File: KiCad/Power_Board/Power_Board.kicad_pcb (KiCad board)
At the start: 4 copper layers, 101.6 x 63.5 mm, 170 parts, among them P1 CONN_LEFT_TOP, P10 CONN_02X01, P2 CONN_RIGHT_TOP, P3 CONN_LEFT_BOTTOM, P4 CONN_RIGHT_BOTTOM, P5 CONN_02X01, P6 CONN_02X01, P7 CONN_02X01, P8 CONN_02X01, P9 CONN_02X01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

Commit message: SPI Trace Cleanup
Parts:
- added ?: , OpenCamera:STITCH_VIA, F.Cu at (102.3, 101.1)
- added ?: , OpenCamera:STITCH_VIA, F.Cu at (101.0, 101.3)
- added ?: , OpenCamera:STITCH_VIA, F.Cu at (99.4, 101.1)
- moved ? 14.0 mm to (144.5, 113.5)
- moved ? 7.57 mm to (146.3, 113.7)
- moved TP4 3.54 mm to (127.2, 123.1)
- moved TP1 2.85 mm to (127.3, 133.4)
- moved ? 2.02 mm to (171.7, 113.7)
- moved TP7 1.31 mm to (161.5, 115.2)
- moved R32 0.52 mm to (159.4, 111.9)
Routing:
- net /Digital_Power/5V: track 45.4 -> 9.83 mm
- net /Analog_Power/-15Va: track 40.3 -> 17.9 mm, vias 2 -> 1
- net /Analog_Power/50Va: track 45.8 -> 31.1 mm, vias 2 -> 1
- net /connectors/L8: track 97.9 -> 91.6 mm
- net /connectors/L6: track 103.7 -> 100.1 mm, vias 2 -> 3
- net /connectors/L5: track 98.4 -> 96.4 mm, vias 3 -> 2
- net /connectors/L9: track 105.4 -> 104.2 mm
- net Net-(C15-Pad1): track 14.8 -> 15.7 mm
- net /connectors/R10: track 16.3 -> 15.7 mm
- net /connectors/R9: track 18.8 -> 18.3 mm
- net Net-(C39-Pad1): track 17.5 -> 18.0 mm

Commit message: More SPI Cleanup.
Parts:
- moved TP7 4.15 mm to (163.9, 111.8)
- moved TP18 1.68 mm to (148.6, 113.2)
- moved TP25 1.37 mm to (156.7, 113.9)
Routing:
- net /connectors/L9: track 104.2 -> 100.3 mm
- net /connectors/L6: track 100.1 -> 101.2 mm
- net /connectors/L5: track 96.4 -> 97.5 mm
- net /connectors/L8: track 91.6 -> 92.6 mm

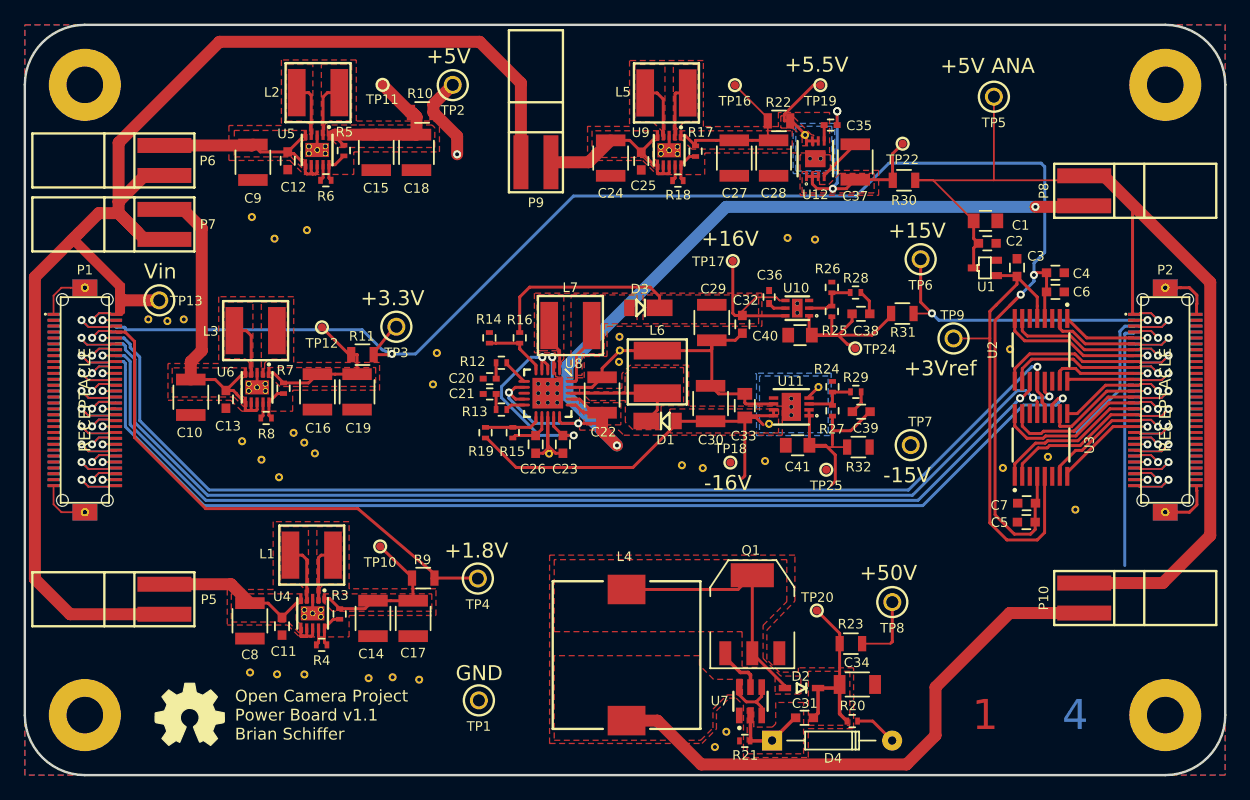
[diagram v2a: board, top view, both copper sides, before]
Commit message: Thickened Power Traces.
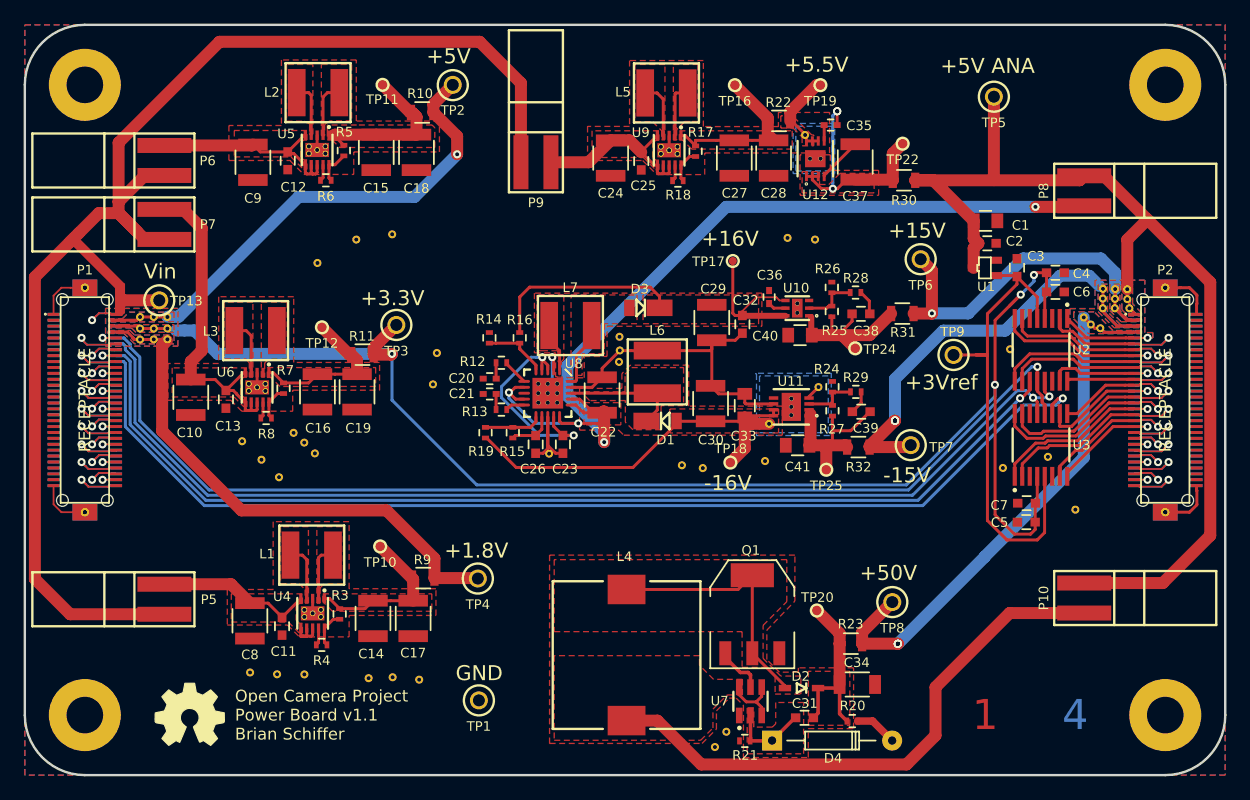
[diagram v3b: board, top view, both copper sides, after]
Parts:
- added ?: , OpenCamera:STITCH_VIA, F.Cu at (179.9, 101.9)
- added ?: , OpenCamera:STITCH_VIA, F.Cu at (182.4, 100.2)
- added ?: , OpenCamera:STITCH_VIA, F.Cu at (182.2, 99.4)
- added ?: , OpenCamera:STITCH_VIA, F.Cu at (101.0, 102.8)
- added ?: , OpenCamera:STITCH_VIA, F.Cu at (99.8, 102.8)
- added ?: , OpenCamera:STITCH_VIA, F.Cu at (98.7, 102.8)
- added ?: , OpenCamera:STITCH_VIA, F.Cu at (101.0, 101.9)
- added ?: , OpenCamera:STITCH_VIA, F.Cu at (99.8, 101.9)
- added ?: , OpenCamera:STITCH_VIA, F.Cu at (98.7, 101.9)
- added ?: , OpenCamera:STITCH_VIA, F.Cu at (179.1, 101.6)
- added ?: , OpenCamera:STITCH_VIA, F.Cu at (178.5, 101.0)
- added ?: , OpenCamera:STITCH_VIA, F.Cu at (180.1, 100.2)
- added ?: , OpenCamera:STITCH_VIA, F.Cu at (180.1, 99.4)
- added ?: , OpenCamera:STITCH_VIA, F.Cu at (180.1, 98.5)
- added ?: , OpenCamera:STITCH_VIA, F.Cu at (182.2, 98.6)
- added ?: , OpenCamera:STITCH_VIA, F.Cu at (181.2, 100.2)
- added ?: , OpenCamera:STITCH_VIA, F.Cu at (181.2, 99.4)
- added ?: , OpenCamera:STITCH_VIA, F.Cu at (181.2, 98.6)
- moved ? 7.22 mm to (120.0, 93.9)
- moved ? 6.92 mm to (117.0, 94.4)
- moved ? 6.78 mm to (113.7, 96.4)
- moved ? 3.70 mm to (98.7, 100.9)
- moved TP9 1.40 mm to (167.5, 104.1)
- moved ? 0.50 mm to (99.8, 100.9)
- moved ? 0.34 mm to (101.0, 100.9)
- moved TP3 0.15 mm to (120.3, 101.6)
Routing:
- net /Digital_Power/5V: track 9.83 -> 42.3 mm, vias 2 -> 1
- net /Analog_Power/-15Va: track 17.9 -> 40.8 mm, vias 1 -> 7
- net /Analog_Power/50Va: track 31.1 -> 50.0 mm, vias 1 -> 4
- net /Digital_Power/3.3V: track 144.1 -> 133.6 mm
- net /Analog_Power/5Va: track 98.4 -> 108.1 mm, vias 1 -> 0
- net Net-(C38-Pad1): track 17.4 -> 26.8 mm
- net Net-(C31-Pad1): track 15.1 -> 22.1 mm
- net Net-(C35-Pad1): track 20.3 -> 26.8 mm
- net Net-(C14-Pad1): track 13.9 -> 19.7 mm
- net /Analog_Power/15Va: track 26.2 -> 31.6 mm, vias 2 -> 1
- net /Analog_Power/5.5V: track 8.47 -> 12.0 mm
- net /Digital_Power/1.8V: track 49.1 -> 46.7 mm, vias 1 -> 0
- net Net-(C16-Pad1): track 13.7 -> 15.7 mm
- net Net-(C39-Pad1): track 18.0 -> 19.7 mm
- net /Analog_Power/-16V: track 36.2 -> 37.6 mm
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- added copper zone on B.Cu, net /Analog_Power/-15Va
- added copper zone on F.Cu, net /Analog_Power/-15Va
- added copper zone on B.Cu, net /Analog_Power/15Va
- added copper zone on F.Cu, net /Analog_Power/15Va
- added copper zone on B.Cu, net /Analog_Power/50Va
- added copper zone on F.Cu, net /Analog_Power/50Va
- added copper zone on B.Cu, net /Analog_Power/5Va
- added copper zone on F.Cu, net /Analog_Power/5Va
- added copper zone on B.Cu, net /Digital_Power/1.8V
- added copper zone on F.Cu, net /Digital_Power/1.8V
- added copper zone on B.Cu, net /Digital_Power/3.3V
- added copper zone on F.Cu, net /Digital_Power/3.3V
- added copper zone on B.Cu, net /Digital_Power/5V
- added copper zone on F.Cu, net /Digital_Power/5V

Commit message: Pulled ground pour back to ensure 20mil clearance to board edge.
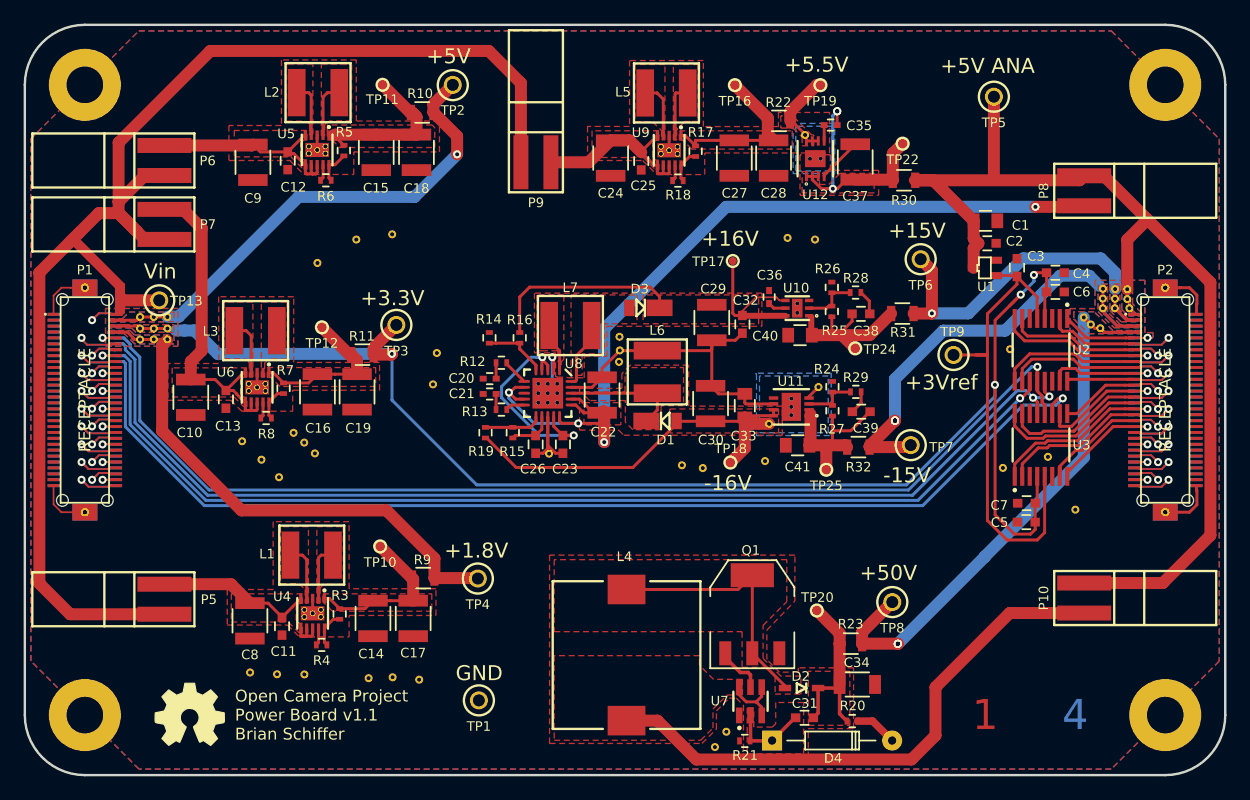
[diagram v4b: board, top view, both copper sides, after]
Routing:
- net Net-(C22-Pad1): track 81.0 -> 78.4 mm
- net /connectors/L1: track 151.5 -> 150.5 mm

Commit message: Placed a bunch of ground plane stitching vias.
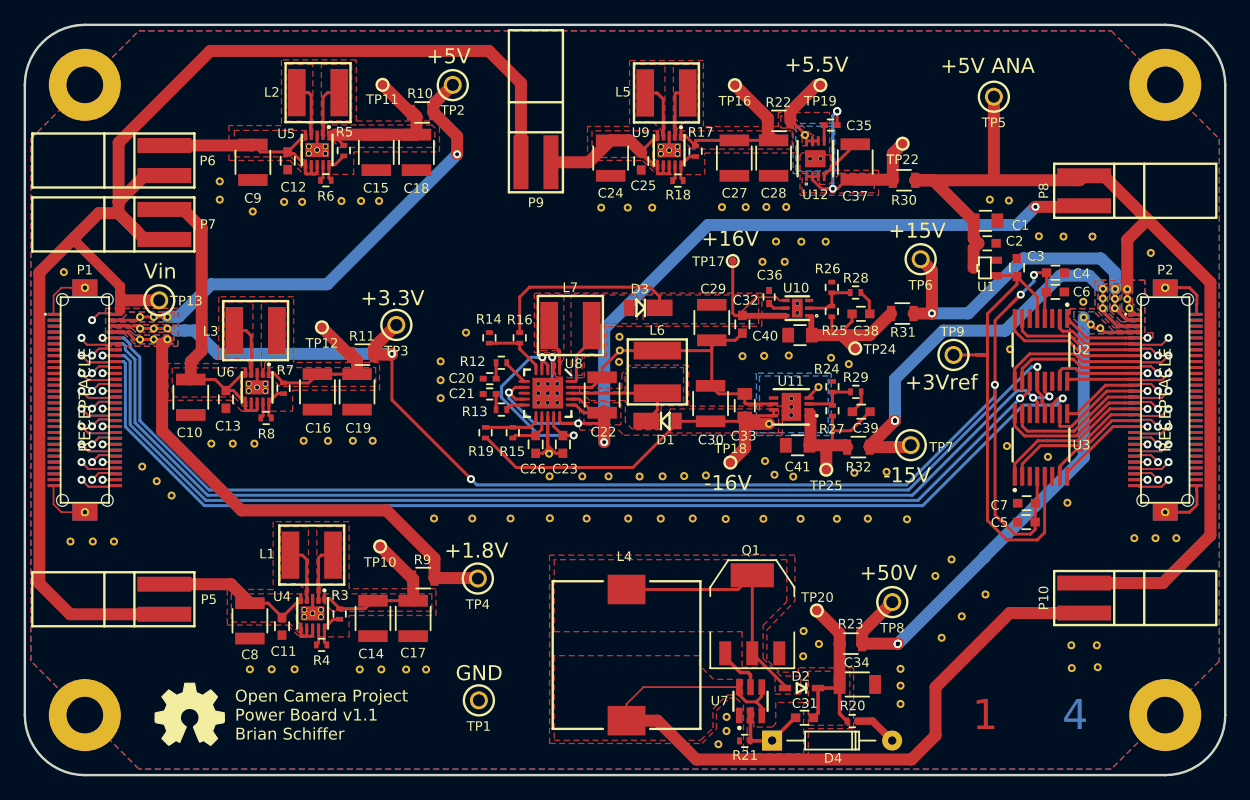
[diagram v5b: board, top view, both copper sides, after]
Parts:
- added ?: , OpenCamera:STITCH_VIA, F.Cu at (172.2, 91.1)
- added ?: , OpenCamera:STITCH_VIA, F.Cu at (172.0, 111.8)
- added ?: , OpenCamera:STITCH_VIA, F.Cu at (94.7, 119.9)
- added ?: , OpenCamera:STITCH_VIA, F.Cu at (96.4, 119.9)
- added ?: , OpenCamera:STITCH_VIA, F.Cu at (92.8, 119.9)
- added ?: , OpenCamera:STITCH_VIA, F.Cu at (182.8, 119.6)
- added ?: , OpenCamera:STITCH_VIA, F.Cu at (184.6, 119.6)
- added ?: , OpenCamera:STITCH_VIA, F.Cu at (186.4, 119.6)
- added ?: , OpenCamera:STITCH_VIA, F.Cu at (179.7, 130.6)
- added ?: , OpenCamera:STITCH_VIA, F.Cu at (177.5, 130.6)
- added ?: , OpenCamera:STITCH_VIA, F.Cu at (179.6, 128.7)
- added ?: , OpenCamera:STITCH_VIA, F.Cu at (170.6, 91.0)
- added ?: , OpenCamera:STITCH_VIA, F.Cu at (177.5, 128.7)
- added ?: , OpenCamera:STITCH_VIA, F.Cu at (163.0, 130.7)
- added ?: , OpenCamera:STITCH_VIA, F.Cu at (163.0, 132.1)
- added ?: , OpenCamera:STITCH_VIA, F.Cu at (163.0, 133.7)
- added ?: , OpenCamera:STITCH_VIA, F.Cu at (156.1, 128.6)
- added ?: , OpenCamera:STITCH_VIA, F.Cu at (154.8, 129.6)
- added ?: , OpenCamera:STITCH_VIA, F.Cu at (154.8, 127.5)
- added ?: , OpenCamera:STITCH_VIA, F.Cu at (148.3, 136.0)
- added ?: , OpenCamera:STITCH_VIA, F.Cu at (121.2, 130.8)
- added ?: , OpenCamera:STITCH_VIA, F.Cu at (153.9, 114.4)
- added ?: , OpenCamera:STITCH_VIA, F.Cu at (92.2, 97.1)
- added ?: , OpenCamera:STITCH_VIA, F.Cu at (157.1, 104.4)
- added ?: , OpenCamera:STITCH_VIA, F.Cu at (158.6, 104.9)
- added ?: , OpenCamera:STITCH_VIA, F.Cu at (153.2, 96.3)
- added ?: , OpenCamera:STITCH_VIA, F.Cu at (153.6, 104.2)
- added ?: , OpenCamera:STITCH_VIA, F.Cu at (151.5, 104.2)
- added ?: , OpenCamera:STITCH_VIA, F.Cu at (149.6, 104.2)
- added ?: , OpenCamera:STITCH_VIA, F.Cu at (156.7, 94.6)
- added ?: , OpenCamera:STITCH_VIA, F.Cu at (151.3, 96.3)
- added ?: , OpenCamera:STITCH_VIA, F.Cu at (153.3, 91.6)
- added ?: , OpenCamera:STITCH_VIA, F.Cu at (151.7, 91.6)
- added ?: , OpenCamera:STITCH_VIA, F.Cu at (184.2, 95.5)
- added ?: , OpenCamera:STITCH_VIA, F.Cu at (149.9, 91.6)
- added ?: , OpenCamera:STITCH_VIA, F.Cu at (147.9, 91.6)
- added ?: , OpenCamera:STITCH_VIA, F.Cu at (110.8, 91.2)
- added ?: , OpenCamera:STITCH_VIA, F.Cu at (142.0, 91.7)
- added ?: , OpenCamera:STITCH_VIA, F.Cu at (139.9, 91.7)
- added ?: , OpenCamera:STITCH_VIA, F.Cu at (137.7, 91.7)
- added ?: , OpenCamera:STITCH_VIA, F.Cu at (118.9, 91.1)
- added ?: , OpenCamera:STITCH_VIA, F.Cu at (108.2, 92.0)
- added ?: , OpenCamera:STITCH_VIA, F.Cu at (105.4, 91.0)
- added ?: , OpenCamera:STITCH_VIA, F.Cu at (105.4, 89.4)
- added ?: , OpenCamera:STITCH_VIA, F.Cu at (178.5, 99.6)
- added ?: , OpenCamera:STITCH_VIA, F.Cu at (101.3, 116.0)
- added ?: , OpenCamera:STITCH_VIA, F.Cu at (100.1, 114.8)
- added ?: , OpenCamera:STITCH_VIA, F.Cu at (98.8, 113.6)
- added ?: , OpenCamera:STITCH_VIA, F.Cu at (170.2, 124.4)
- added ?: , OpenCamera:STITCH_VIA, F.Cu at (167.3, 121.5)
- added ?: , OpenCamera:STITCH_VIA, F.Cu at (166.0, 122.8)
- added ?: , OpenCamera:STITCH_VIA, F.Cu at (163.6, 118.0)
- added ?: , OpenCamera:STITCH_VIA, F.Cu at (161.8, 114.0)
- added ?: , OpenCamera:STITCH_VIA, F.Cu at (159.1, 114.1)
- added ?: , OpenCamera:STITCH_VIA, F.Cu at (152.3, 114.3)
- added ?: , OpenCamera:STITCH_VIA, F.Cu at (179.3, 94.1)
- added ?: , OpenCamera:STITCH_VIA, F.Cu at (145.4, 118.0)
- added ?: , OpenCamera:STITCH_VIA, F.Cu at (160.2, 118.0)
- added ?: , OpenCamera:STITCH_VIA, F.Cu at (157.6, 118.0)
- added ?: , OpenCamera:STITCH_VIA, F.Cu at (142.7, 118.0)
- added ?: , OpenCamera:STITCH_VIA, F.Cu at (142.9, 114.4)
- added ?: , OpenCamera:STITCH_VIA, F.Cu at (140.9, 114.4)
- added ?: , OpenCamera:STITCH_VIA, F.Cu at (138.3, 114.4)
- added ?: , OpenCamera:STITCH_VIA, F.Cu at (136.1, 114.4)
- added ?: , OpenCamera:STITCH_VIA, F.Cu at (133.3, 114.4)
- added ?: , OpenCamera:STITCH_VIA, F.Cu at (126.2, 102.2)
- added ?: , OpenCamera:STITCH_VIA, F.Cu at (176.8, 94.1)
- added ?: , OpenCamera:STITCH_VIA, F.Cu at (124.1, 107.8)
- added ?: , OpenCamera:STITCH_VIA, F.Cu at (114.6, 111.4)
- added ?: , OpenCamera:STITCH_VIA, F.Cu at (148.2, 118.0)
- added ?: , OpenCamera:STITCH_VIA, F.Cu at (123.5, 118.0)
- added ?: , OpenCamera:STITCH_VIA, F.Cu at (133.3, 118.0)
- added ?: , OpenCamera:STITCH_VIA, F.Cu at (154.6, 118.0)
- added ?: , OpenCamera:STITCH_VIA, F.Cu at (151.4, 118.0)
- added ?: , OpenCamera:STITCH_VIA, F.Cu at (140.0, 118.0)
- added ?: , OpenCamera:STITCH_VIA, F.Cu at (136.4, 118.0)
- added ?: , OpenCamera:STITCH_VIA, F.Cu at (130.0, 118.0)
- added ?: , OpenCamera:STITCH_VIA, F.Cu at (174.7, 94.1)
- added ?: , OpenCamera:STITCH_VIA, F.Cu at (126.8, 118.0)
- added ?: , OpenCamera:STITCH_VIA, F.Cu at (166.5, 128.1)
- moved ? 13.0 mm to (168.2, 126.3)
- moved ? 8.10 mm to (112.4, 91.2)
- moved ? 6.42 mm to (117.4, 91.1)
- moved ? 5.00 mm to (118.3, 111.4)
- moved ? 4.12 mm to (116.7, 111.4)
- moved ? 3.53 mm to (108.3, 111.6)
- moved ? 3.50 mm to (115.7, 91.1)
- moved ? 2.78 mm to (106.5, 111.6)
- moved ? 2.61 mm to (104.7, 111.6)
- moved ? 1.26 mm to (148.3, 134.8)
- moved ? 1.17 mm to (154.6, 94.6)
- moved ? 1.16 mm to (119.1, 130.8)
- moved ? 1.08 mm to (112.5, 111.4)
- moved ? 1.05 mm to (117.2, 130.8)
- moved ? 1.04 mm to (122.9, 130.8)
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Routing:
- net Net-(L4-Pad1): track 52.7 -> 64.3 mm
- net /Digital_Power/3.3V: vias 4 -> 5

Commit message: Fixed missing links between ground vias for some of the thermal pads.
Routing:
- net GND: track 74.1 -> 81.6 mm
